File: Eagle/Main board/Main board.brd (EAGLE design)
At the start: 160 x 160 mm, 123 parts, among them IC1 LMZ14202TZE-ADJ_NOPB, IC2 VNH7070ASTR, IC3 VNH7070ASTR, IC4 VNH7070ASTR, IC5 VNH7070ASTR, IC6 ATMEGA32U4-AU, J3 43650-0201, J4 43650-0201, J5 43650-0201, J6 43650-0201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

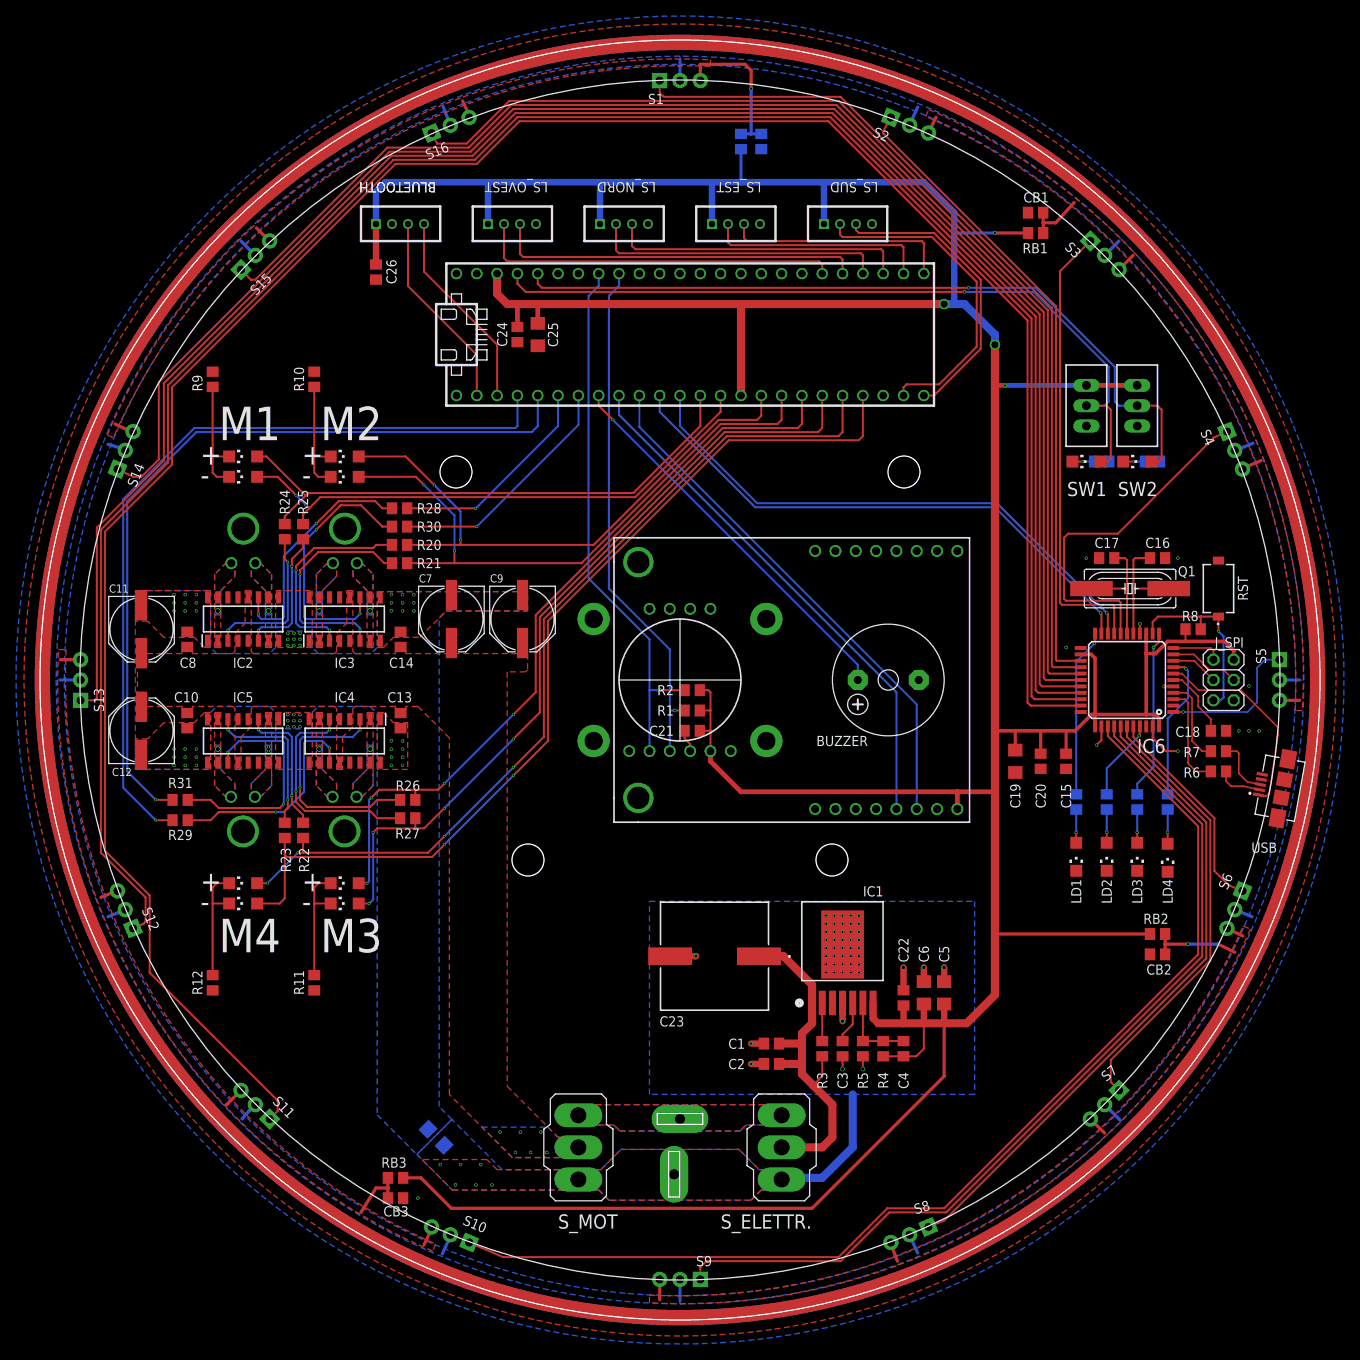
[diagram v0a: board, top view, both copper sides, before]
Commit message: Added RCWL compatible ToF
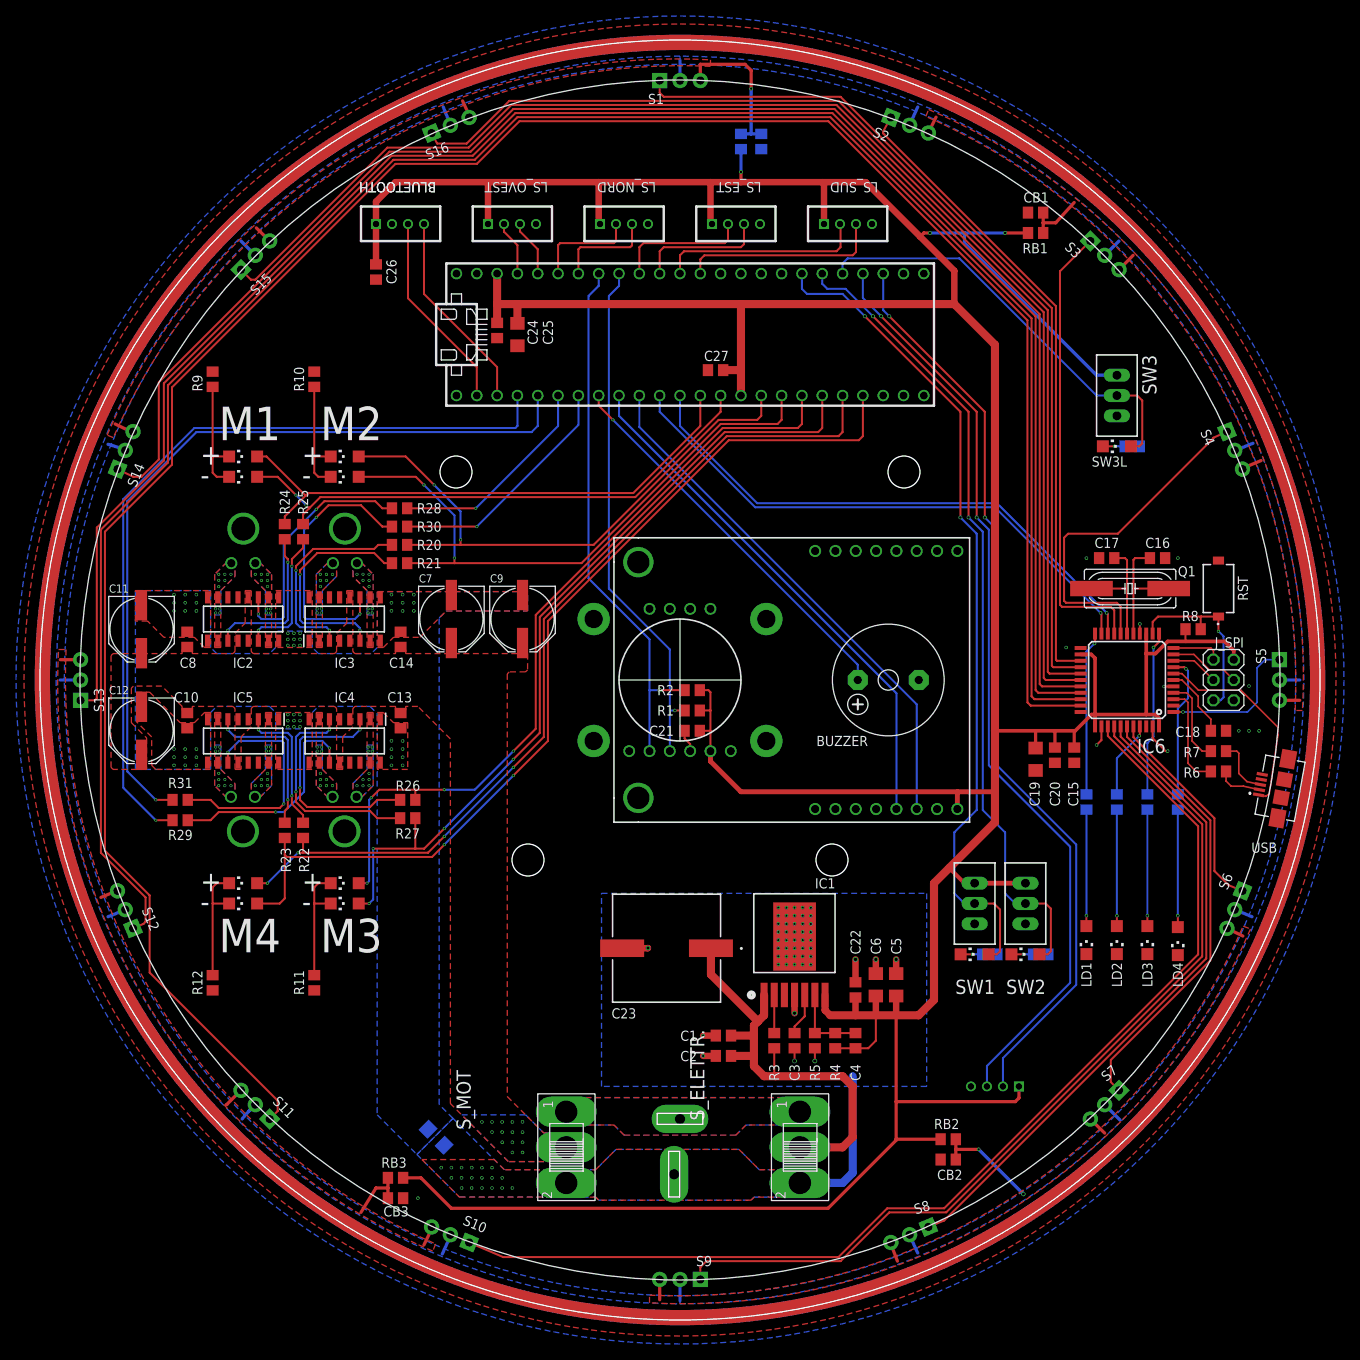
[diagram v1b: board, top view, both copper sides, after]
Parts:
- added C27: 100n, rcl:C0805
- added R32: (no value), rcl:R0805
- added SW3: TL38PO, switch:TL3XPO
- added SW3L: (no value), led:CHIPLED_1206
- added TOF: TWIG_2.0, CONNECTER:2.0_1X4
- S_ELETTR., S_MOT: device switch:320-916 -> Switch:255SB
- moved SW1 63.8 mm to (36.8, -27.9)
- moved SW2 63.8 mm to (43.2, -27.9)
- moved R13 63.2 mm to (38.7, -34.3)
- moved R14 63.2 mm to (45.1, -34.3)
- moved SW1L 63.2 mm to (36.8, -34.3)
- moved SW2L 63.2 mm to (43.2, -34.3)
- moved CB2 36.6 mm to (33.5, -59.9)
- moved RB2 36.6 mm to (33.5, -57.4)
- moved LD1 10.5 mm to (50.8, -32.5)
- moved LD2 10.5 mm to (54.6, -32.5)
- moved LD3 10.5 mm to (58.4, -32.5)
- moved LD4 10.5 mm to (62.2, -32.6)
- moved S_MOT 8.74 mm to (-17.8, -51.3), turned to 270 degrees
- moved S_ELETTR. 7.22 mm to (11.4, -51.3), turned to 270 degrees
- moved C5 6.08 mm to (27.0, -38.1)
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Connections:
- removed net BPS: U$1.39/A20
- removed net KICK: U$1.20/A6
- removed net ROLL: U$1.21/A7
- new net A/TRIG: TOF.2, U$1.35/A16
- new net ECHO: TOF.3, U$1.36/A17
- new net SW3: SW3.2, SW3L.A, U$1.37/A18
- net +3V3: now also C27.1, SW3.1, TOF.1
- net E_EST: now also U$1.16/A2; no longer U$1.33/A14
- net E_INT: now also U$1.17/A3; no longer U$1.34/A15
- net GND: now also C27.2, R32.2, SW3.3, TOF.4
- net N$19: now also R32.1, SW3L.C; no longer U$1.30
- net N_EST: now also U$1.20/A6; no longer U$1.35/A16
- net N_INT: now also U$1.21/A7; no longer U$1.36/A17
- net O_EST: now also U$1.22/A8; no longer U$1.37/A18
- net O_INT: now also U$1.23/A9; no longer U$1.38/A19
- net SW1: now also U$1.39/A20; no longer U$1.23/A9
- net SW2: now also U$1.38/A19; no longer U$1.22/A8
- net S_EST: now also U$1.14/A0; no longer U$1.32/A13
- net S_INT: now also U$1.15/A1; no longer U$1.31/A12
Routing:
- net ECHO: track 0.00 -> 116.6 mm, vias 0 -> 2
- net A/TRIG: track 0.00 -> 115.4 mm, vias 0 -> 2
- net SW3: track 0.00 -> 53.3 mm
- net O_EST: track 46.1 -> 7.12 mm
- net O_INT: track 45.5 -> 6.90 mm
- net N_EST: track 37.2 -> 12.6 mm
- net +3V3: track 568.1 -> 591.8 mm, vias 4 -> 3
- net N_INT: track 36.7 -> 13.1 mm
- net S_INT: track 41.2 -> 25.7 mm
- net E_EST: track 28.3 -> 16.2 mm
- net S_EST: track 37.1 -> 25.1 mm
- net +12V: track 46.0 -> 57.2 mm
- net E_INT: track 27.8 -> 16.7 mm
- net N$22: track 4.16 -> 14.6 mm
- net N$21: track 4.16 -> 14.6 mm
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
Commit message: Main board done
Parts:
- added BALL, MULTI1, MULTI2: TWIG_2.0, CONNECTER:2.0_1X4
- added BAT, ELECT, MOT: (no value), led:CHIPLED_1206
- added C28: EEV-FK1C152Q, Panasonic 1500uF:FKV(H13)
- added J2, J7: 43650-0201, Molex motori:43650-0200
- added R33, R34, R35: (no value), rcl:R0805
- moved R32 6.00 mm to (56.5, 35.2)
- moved SW3 6.00 mm to (54.6, 41.6)
- moved SW3L 6.00 mm to (54.6, 35.2)
- moved C23 4.32 mm to (-1.91, -29.2)
- moved C2 3.82 mm to (5.75, -43.2), flipped to the bottom, turned to 0 degrees
- moved R11 2.08 mm to (-47.0, -36.2), turned to 0 degrees
- moved R12 2.08 mm to (-59.7, -36.2), turned to 0 degrees
- moved C1 1.31 mm to (5.75, -45.7), flipped to the bottom, turned to 0 degrees
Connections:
- new net BALL_IN: BALL.2, U$1.32/A13
- new net BALL_OUT: BALL.3, U$1.A22/DAC1
- new net MULTI_DIG1: MULTI1.3, U$1.31/A12
- new net MULTI_DIG2: MULTI2.3, U$1.34/A15
- new net MULTI_PWM1: MULTI1.2, U$1.30
- new net MULTI_PWM2: MULTI2.2, U$1.35/A16
- new net N$24: BAT.A, R33.2
- new net N$25: MOT.A, R34.2
- new net N$26: ELECT.A, R35.1
- net +3V3: now also BALL.1, MULTI1.1, MULTI2.1, R35.2
- net A/TRIG: now also U$1.36/A17; no longer U$1.35/A16
- net ECHO: now also U$1.37/A18; no longer U$1.36/A17
- net GND: now also BALL.4, BAT.C, ELECT.C, MOT.C, MULTI1.4, MULTI2.4
- net SW3: now also U$1.33/A14; no longer U$1.37/A18
- net V-: now also C28.2, J2.2, J7.2
- net VBAT+: now also R33.1
- net VMOT: now also C28.1, J2.1, J7.1, R34.1
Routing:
- net MULTI_DIG1: track 0.00 -> 183.8 mm, vias 0 -> 2
- net MULTI_PWM1: track 0.00 -> 181.3 mm, vias 0 -> 2
- net MULTI_DIG2: track 0.00 -> 180.8 mm
- net MULTI_PWM2: track 0.00 -> 177.4 mm
- net BALL_OUT: track 0.00 -> 60.6 mm
- net +3V3: track 591.8 -> 639.0 mm, vias 3 -> 5
- net VBAT+: track 0.00 -> 36.1 mm, vias 0 -> 2
- net VMOT: track 0.00 -> 33.9 mm, vias 14 -> 15
- net BALL_IN: track 0.00 -> 27.5 mm
- net SW3: track 53.3 -> 38.3 mm
- net +12V: track 57.2 -> 60.9 mm, vias 0 -> 2
- net M4_PWM: track 99.9 -> 96.3 mm
- net M3_PWM: track 100.8 -> 97.2 mm
- net N$24: track 0.00 -> 3.40 mm, vias 0 -> 1
- net N$26: track 0.00 -> 3.40 mm, vias 0 -> 1
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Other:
- board text added: "MULTI1"
- board text added: "MULTI2"
- board text added: "PALLA_PRESA"

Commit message: Job finished. Ready to print
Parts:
- removed R19: (no value), rcl:R1206
- added TOF_TOP: TWIG_2.0, CONNECTER:2.0_1X4
- moved TOF 9.04 mm to (30.5, -49.1)
- moved RST 4.94 mm to (70.7, 7.87), turned to 0 degrees
- moved Q1 1.02 mm to (56.3, 10.4)
- moved R14 1.00 mm to (46.1, -34.3)
- moved SW2 1.00 mm to (44.2, -27.9)
- moved SW2L 1.00 mm to (44.2, -34.3)
- moved C16 0.92 mm to (58.9, 14.7)
- moved C17 0.57 mm to (53.6, 14.7)
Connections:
- net +3V3: now also TOF_TOP.1
- net A/TRIG: now also TOF_TOP.2
- net ECHO: now also TOF_TOP.3
- net GND: now also TOF_TOP.4; no longer R19.2
- net V-: no longer R19.1
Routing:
- net A/TRIG: track 116.4 -> 127.1 mm
- net ECHO: track 118.6 -> 127.7 mm, vias 2 -> 3
- net +3V3: track 639.0 -> 636.0 mm
- net N$6: track 15.8 -> 14.5 mm
- net N$5: track 15.3 -> 14.6 mm
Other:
- outline, holes or cut-outs redrawn
- board text added: "Aco"
- board text added: "DVDSPACCA"
- board text added: "Designed by Dario Casagrande"
- board text added: "EmaMaker"
- board text added: "Made with love by SPQR team:"
- board text added: "Morco"
- board text added: "Siria"
- board text added: "TOF"
- board text added: "eooooooooooooooo"
- board text added: "latino_deluxe"
